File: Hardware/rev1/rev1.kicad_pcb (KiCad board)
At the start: 4 copper layers, 80 x 22 mm, 44 parts, among them J1 Conn_ARM_JTAG_SWD_10, J2 USB_C_Receptacle_USB2.0_14P, J3 Screw_Terminal_01x02, J4 Conn_01x18_Socket, J5 Conn_01x18_Socket, Q1 AO3400A, SW1 SW_Push, U1 W25Q128JVS, U2 HT75xx-1-SOT89, U3 MS5607-02BA, U4 STM32F103C8Tx, Y1 16MHz

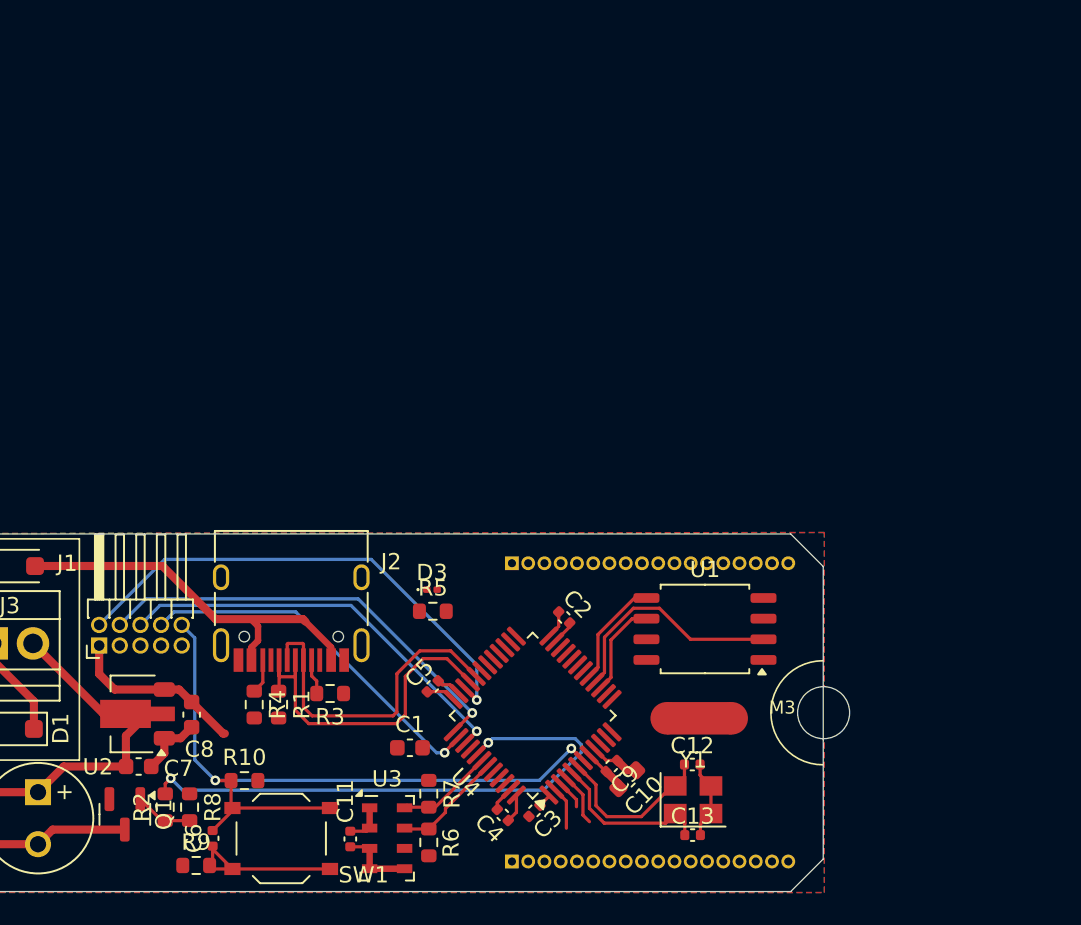
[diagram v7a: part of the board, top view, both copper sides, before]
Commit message: Defucked the header net assignments, cleaned up schematic sheet, routed to headers
routing is uninformed, took care to allow ground planes to not become islands however there are some sketchy looking bits. Power still requires routing and we are really tight on space so will likely either need to redo all those traces for priority for 3.3V or weave power in between them
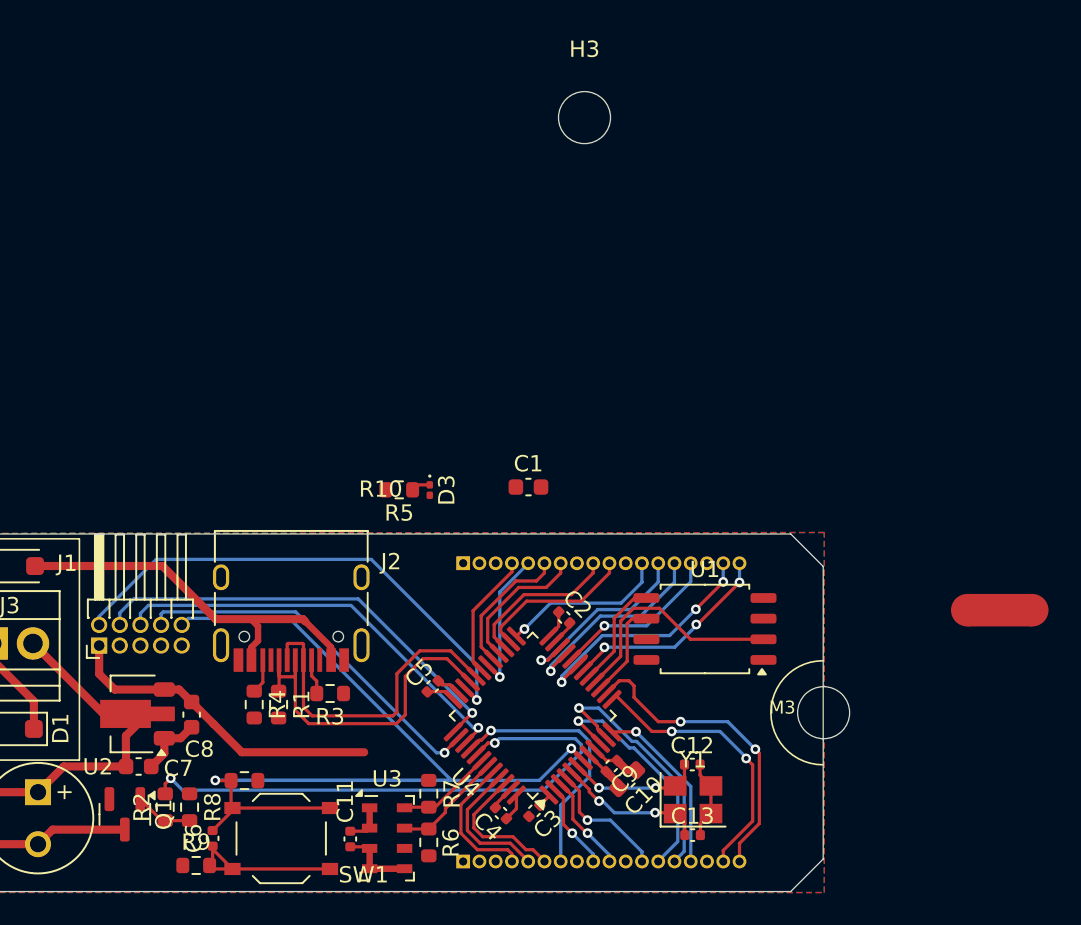
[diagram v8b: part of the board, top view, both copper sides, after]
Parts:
- added H3: MountingHole, MountingHole:MountingHole_3.2mm_M3, F.Cu at (178.5, 92.6)
- moved NT1 19.6 mm to (204.0, 122.9)
- moved C1 17.6 mm to (175.0, 115.3)
- moved R5 7.75 mm to (167.1, 115.5), turned to 180 degrees
- moved D3 6.13 mm to (168.9, 115.5), turned to -90 degrees
- moved J4 3.00 mm to (171.0, 120.0)
- moved J5 3.00 mm to (171.0, 138.3)
- moved C4 0.16 mm to (173.3, 135.4)
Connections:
- J4 pad 1: /Microcontroller/PC13 -> VBUS
- J4 pad 10: /Microcontroller/PA4 -> /Microcontroller/PB13
- J4 pad 12: /Microcontroller/PB0 -> /Microcontroller/PB12
- J4 pad 13: /Microcontroller/PB1 -> /Microcontroller/PB11
- J4 pad 14: /Microcontroller/PB2 -> /Microcontroller/PB10
- J4 pad 15: /Microcontroller/PB10 -> /Microcontroller/PB2
- J4 pad 17: +3.3V -> /Microcontroller/PB1
- J4 pad 18: VBUS -> /Microcontroller/PB0
- J4 pad 2: /Microcontroller/PC14 -> +3.3V
- J4 pad 4: /Microcontroller/PC15 -> /Microcontroller/PA10
- J4 pad 5: /Microcontroller/PA0 -> /Microcontroller/PA9
- J4 pad 6: /Microcontroller/PA1 -> /Microcontroller/PA8
- J4 pad 7: /Microcontroller/PA2 -> /Microcontroller/PB15
- J4 pad 9: /Microcontroller/PA3 -> /Microcontroller/PB14
- J5 pad 1: /Microcontroller/PB11 -> VBUS
- J5 pad 10: /Microcontroller/PA10 -> /Microcontroller/PC14
- J5 pad 12: /Microcontroller/PB4 -> /Microcontroller/PC15
- J5 pad 13: /Microcontroller/BOOTO -> /Microcontroller/PA0
- J5 pad 14: /Microcontroller/PB8 -> /Microcontroller/PA1
- J5 pad 15: /Microcontroller/PB9 -> /Microcontroller/PA2
- J5 pad 17: +3.3V -> /Microcontroller/PA3
- J5 pad 18: VBUS -> /Microcontroller/PA4
- J5 pad 2: /Microcontroller/PB12 -> +3.3V
- J5 pad 4: /Microcontroller/PB13 -> /Microcontroller/BOOTO
- J5 pad 5: /Microcontroller/PB14 -> /Microcontroller/PB8
- J5 pad 6: /Microcontroller/PB15 -> /Microcontroller/PB9
- J5 pad 7: /Microcontroller/PA8 -> /Microcontroller/PB4
- J5 pad 9: /Microcontroller/PA9 -> /Microcontroller/PC13
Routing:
- net /Microcontroller/DBG.NRESET: track 44.8 -> 69.8 mm
- net /Microcontroller/PA4: track 0.00 -> 19.2 mm, vias 0 -> 2
- net /Microcontroller/PA3: track 0.00 -> 17.2 mm, vias 0 -> 2
- net /Microcontroller/PB1: track 0.00 -> 16.9 mm, vias 0 -> 3
- net /Microcontroller/PB4: track 0.00 -> 16.2 mm, vias 0 -> 1
- net /Microcontroller/PA1: track 0.00 -> 15.8 mm, vias 0 -> 1
- net /Microcontroller/PA0: track 0.00 -> 14.6 mm, vias 0 -> 1
- net /Microcontroller/PB0: track 0.00 -> 13.2 mm, vias 0 -> 3
- net /Microcontroller/PB10: track 0.00 -> 12.7 mm, vias 0 -> 1
- net /Microcontroller/PB11: track 0.00 -> 11.9 mm, vias 0 -> 1
- net /Microcontroller/PA2: track 0.00 -> 10.9 mm, vias 0 -> 1
- net /Microcontroller/PB2: track 0.00 -> 10.5 mm, vias 0 -> 1
- net /Microcontroller/PB12: track 0.00 -> 10.3 mm, vias 0 -> 1
- net /Microcontroller/PB13: track 0.00 -> 9.84 mm
- net /Microcontroller/PB14: track 0.00 -> 9.71 mm
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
